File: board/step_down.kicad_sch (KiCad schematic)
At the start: 10 parts, among them U1 AP63200WU

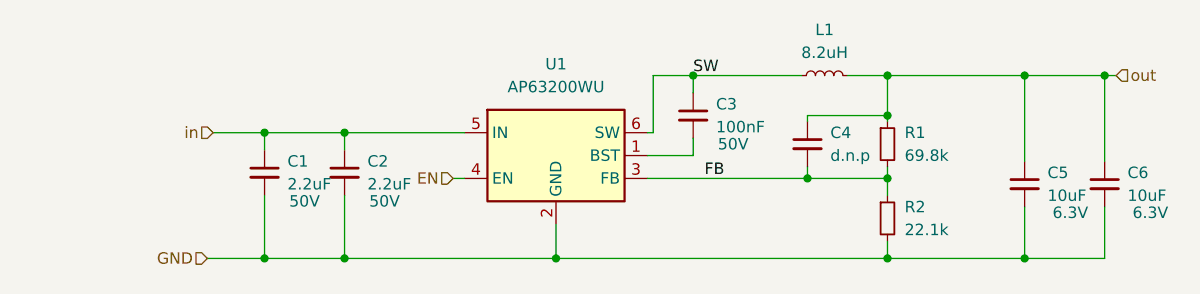
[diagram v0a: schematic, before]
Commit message: used lower dc resistance inductor
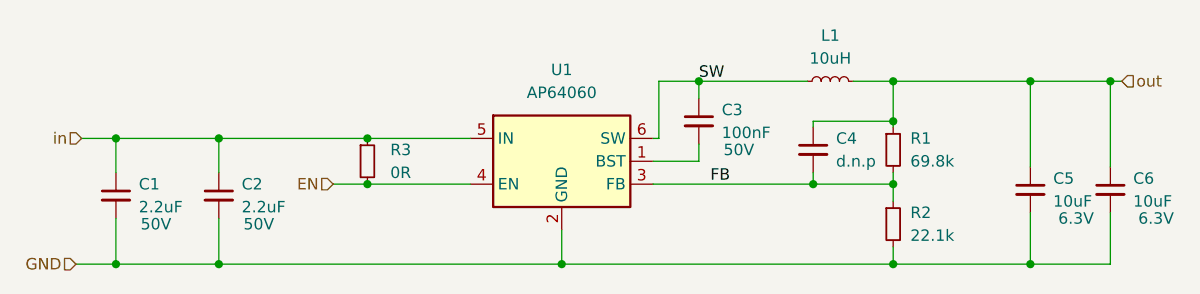
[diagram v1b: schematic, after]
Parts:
- added R3: 0R, Resistor_SMD:R_0402_1005Metric, symbol Device:R_Small
- L1: value 8.2uH -> 10uH; footprint Inductor_SMD:L_1008_2520Metric -> Inductor_SMD:L_1210_3225Metric; Digi-Key_PN 490-13045-1-ND -> (none); MPN DFE252012F-8R2M=P2 -> CBC3225T100KR
- U1: value AP63200WU -> AP64060
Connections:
- net EN: now also R3.2
- net in: now also R3.1
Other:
- moved on the sheet: C1, C2, C3, C4, C5, C6, L1, R1, R2, U1
